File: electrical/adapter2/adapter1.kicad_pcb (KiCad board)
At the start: 2 copper layers, 56.8 x 90 mm, 38 parts, among them J2 Conn_01x08_Pin, J3 0.5 mm, 24P, J4 0.5 mm, 24P, Q1 BSS138, Q2 AO3401A, Q3 S8050 SMD

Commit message: add link and description, adjust zones a bit
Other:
- board text added: "E-Paper adapter for Framework 16, v2 https://github.com/BBBSnowball/fw16 -- snowball"
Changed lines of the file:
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@@
     (property "ki_keywords" "R res resistor")
     (attr smd)
-    (fp_text reference "R10" (at 0 -1.65 90) (layer "F.SilkS")
+    (fp_text reference "R10" (at -3.5 0 90) (layer "F.SilkS")
         (effects (font (size 1 1) (thickness 0.15)))
     )
@@
     (effects (font (size 1 1) (thickness 0.1)) (justify left bottom mirror))
   )
+  (gr_text "E-Paper adapter for Framework 16, v2\nhttps://github.com/BBBSnowball/fw16\n-- snowball" (at 123.25 79.25 270) (layer "B.SilkS")
+    (effects (font (size 1 1) (thickness 0.2) bold) (justify left bottom mirror))
+  )
   (gr_text "add stiffener and\ngoldfingers here,\nplease" (at 126.75 110.5 270) (layer "B.SilkS")
     (effects (font (size 1 1) (thickness 0.1)) (justify left bottom mirror))
@@
     (effects (font (size 1 1) (thickness 0.2)) (justify left bottom))
   )
+  (gr_text "E-Paper adapter for Framework 16, v2\nhttps://github.com/BBBSnowball/fw16\n              -- snowball" (at 126.25 80.75 90) (layer "F.SilkS")
+    (effects (font (size 1 1) (thickness 0.2) bold) (justify left bottom))
+  )
   (gr_text "nSLEEP" (at 131.2 79.3 90) (layer "F.SilkS")
     (effects (font (size 1 1) (thickness 0.2)) (justify left bottom))
@@
         (xy 119.5 45)
         (xy 131.5 45)
-        (xy 131.5 82.25)
-        (xy 119.5 82.25)
+        (xy 131.5 81.25)
+        (xy 119.5 81.25)
       )
     )
@@
         (xy 125.5 79)
         (xy 127.25 80.25)
-        (xy 127.25 82.25)
-        (xy 119.5 82.25)
+        (xy 127.25 81.25)
+        (xy 119.5 81.25)
         (xy 119.5 40.5)
       )
@@
         (xy 131.5 40.5)
         (xy 125.5 40.5)
-        (xy 125.5 82.25)
-        (xy 131.5 82.25)
+        (xy 125.5 81.25)
+        (xy 131.5 81.25)
       )
     )

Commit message: add ATECC608
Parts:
- added C13: 100n, Capacitor_SMD:C_0805_2012Metric_Pad1.18x1.45mm_HandSolder, B.Cu at (137.5, 120.2)
- added U2: ATECC608B-SSHDA, Package_SO:SOIC-8_3.9x4.9mm_P1.27mm, B.Cu at (133.8, 120.5)
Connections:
- U1 pad 12: unconnected-(U1-Pad12) -> /SDA
- U1 pad 13: unconnected-(U1-Pad13) -> /SCL
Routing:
- net GND: track 314.3 -> 352.9 mm, vias 12 -> 13
- net /3V3_RPI: track 11.8 -> 39.1 mm
- net /SDA: track 0.00 -> 7.83 mm
- net /SCL: track 0.00 -> 6.66 mm
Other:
- outline, holes or cut-outs redrawn

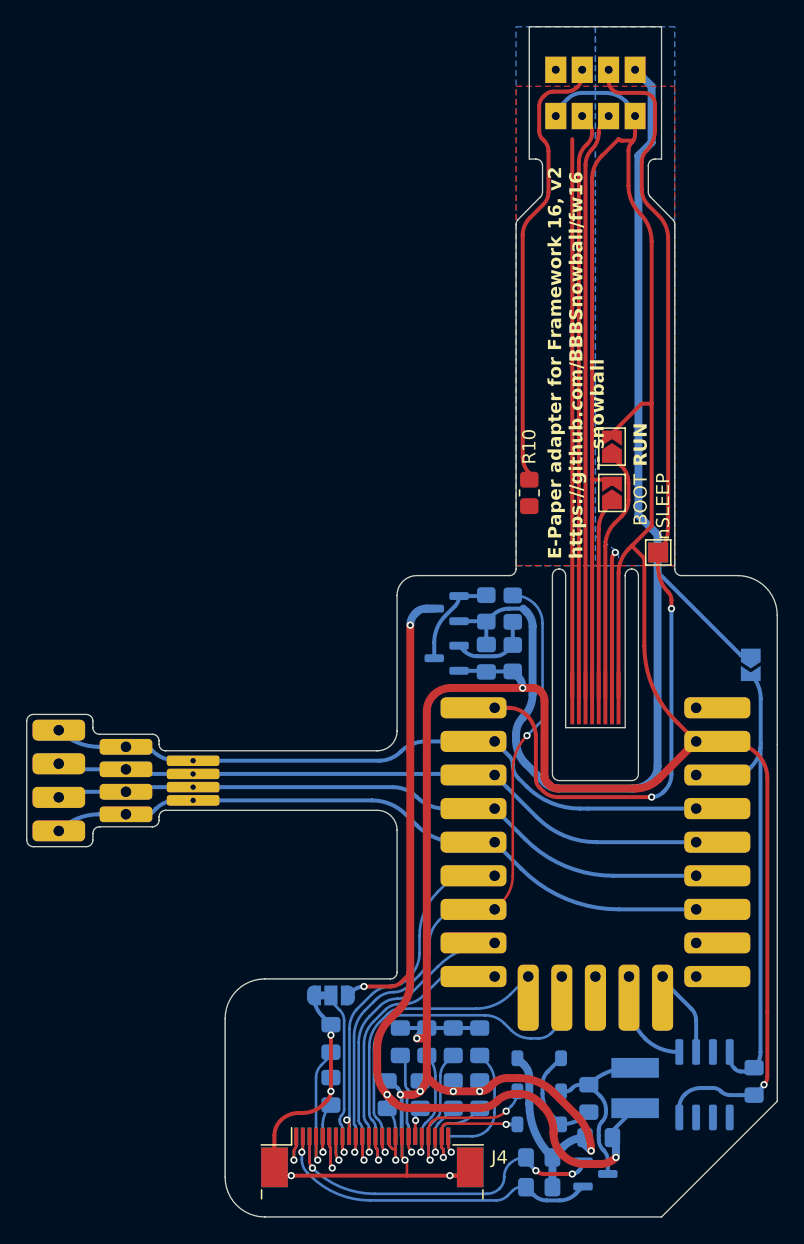
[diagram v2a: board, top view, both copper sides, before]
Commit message: improve pad (solder mask) to copper clearance
JLC say that it should be at least 0.25 mm.
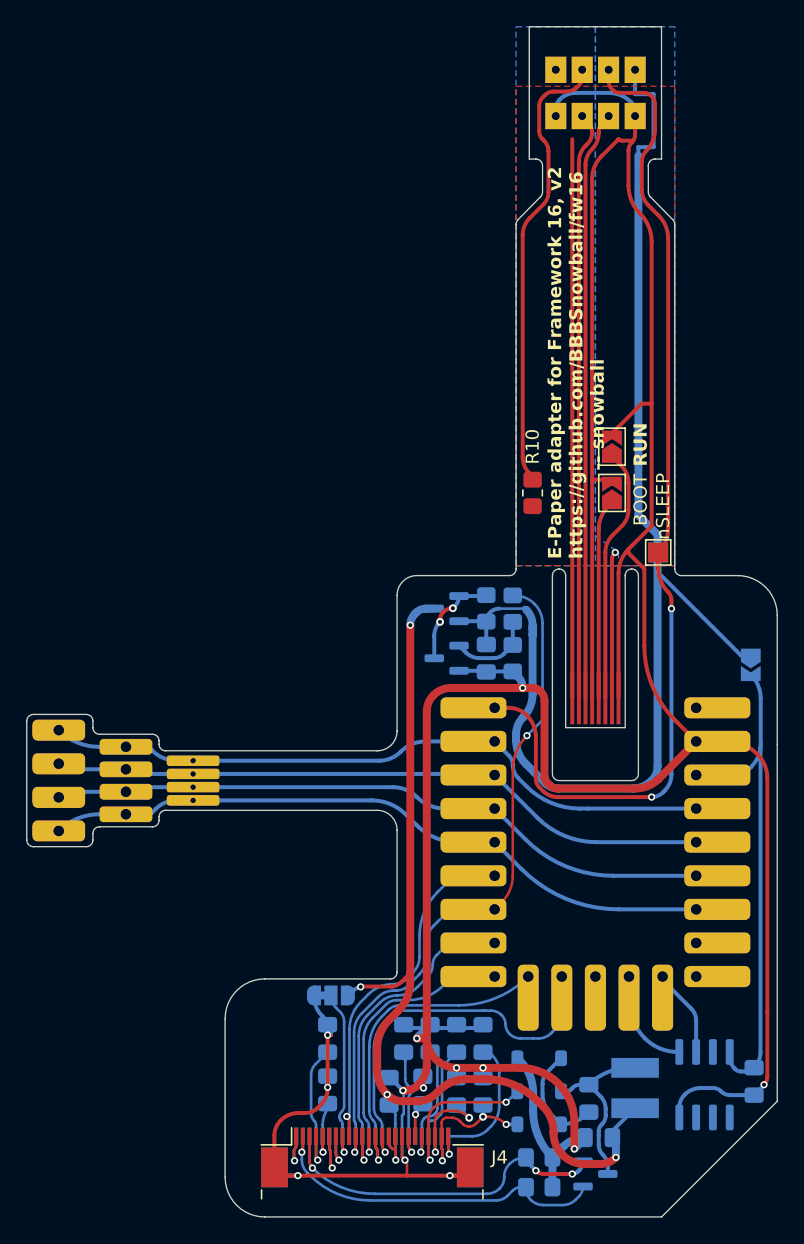
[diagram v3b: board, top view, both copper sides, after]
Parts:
- moved C7 0.40 mm to (112.5, 120.9)
- moved C10 0.35 mm to (115.0, 121.0)
- moved C11 0.35 mm to (117.0, 121.0)
- moved C12 0.35 mm to (117.0, 117.0)
- moved C5 0.35 mm to (111.0, 117.0)
- moved C8 0.35 mm to (113.0, 117.0)
- moved C9 0.35 mm to (115.0, 117.0)
- moved C3 0.29 mm to (109.9, 121.0)
- moved C2 0.27 mm to (105.2, 120.9)
- moved C1 0.25 mm to (105.2, 117.0)
- moved R10 0.25 mm to (120.8, 75.8)
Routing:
- net Net-(J3-Pin_3): track 5.06 -> 8.05 mm, vias 1 -> 2
- net +3V3: track 96.3 -> 98.8 mm
- net /PREVGL: track 13.8 -> 12.2 mm, vias 2 -> 3
- net /BUSY: track 29.1 -> 27.7 mm
- net /DIN: track 29.5 -> 30.6 mm
- net Net-(J3-Pin_1): track 11.7 -> 12.7 mm
- net /PREVGH: track 19.2 -> 20.1 mm
- net /DC: track 24.4 -> 25.2 mm
- net /GDR: track 26.5 -> 27.4 mm
- net GND: track 352.9 -> 353.6 mm
- net /3V3_EP: track 79.3 -> 78.8 mm
- net Net-(Q2-G): track 7.38 -> 7.64 mm, vias 0 -> 2
